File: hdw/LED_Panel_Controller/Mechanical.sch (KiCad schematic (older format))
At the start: 12 parts

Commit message: added digikey pns, footprints, bom scrubbed
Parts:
- MK? (x8): Configuration (none) -> DEV
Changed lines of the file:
@@
 F 3 "" H 4070 3910 50  0001 C CNN
 F 4 "1772-1220-ND" H 4070 3560 50  0001 C CNN "Digi-Key PN"
+F 5 "DEV" H 4070 3560 50  0001 C CNN "Configuration"
 	1    4070 3560
 	1    0    0    -1
@@
 F 3 "" H 4820 3910 50  0001 C CNN
 F 4 "1772-1220-ND" H 4820 3560 50  0001 C CNN "Digi-Key PN"
+F 5 "DEV" H 4820 3560 50  0001 C CNN "Configuration"
 	1    4820 3560
 	1    0    0    -1
@@
 F 3 "" H 4070 4410 50  0001 C CNN
 F 4 "1772-1220-ND" H 4070 4060 50  0001 C CNN "Digi-Key PN"
+F 5 "DEV" H 4070 4060 50  0001 C CNN "Configuration"
 	1    4070 4060
 	1    0    0    -1
@@
 F 3 "" H 4820 4410 50  0001 C CNN
 F 4 "1772-1220-ND" H 4820 4060 50  0001 C CNN "Digi-Key PN"
+F 5 "DEV" H 4820 4060 50  0001 C CNN "Configuration"
 	1    4820 4060
 	1    0    0    -1
@@
 F 3 "" H 4070 5920 50  0001 C CNN
 F 4 "36-9900-ND" H 4070 5670 50  0001 C CNN "Digi-Key PN"
+F 5 "DEV" H 4070 5670 50  0001 C CNN "Configuration"
 	1    4070 5670
 	1    0    0    -1
@@
 F 3 "" H 4820 5920 50  0001 C CNN
 F 4 "36-9900-ND" H 4820 5670 50  0001 C CNN "Digi-Key PN"
+F 5 "DEV" H 4820 5670 50  0001 C CNN "Configuration"
 	1    4820 5670
 	1    0    0    -1
@@
 F 3 "" H 4070 6420 50  0001 C CNN
 F 4 "36-9900-ND" H 4070 6170 50  0001 C CNN "Digi-Key PN"
+F 5 "DEV" H 4070 6170 50  0001 C CNN "Configuration"
 	1    4070 6170
 	1    0    0    -1
@@
 F 3 "" H 4820 6420 50  0001 C CNN
 F 4 "36-9900-ND" H 4820 6170 50  0001 C CNN "Digi-Key PN"
+F 5 "DEV" H 4820 6170 50  0001 C CNN "Configuration"
 	1    4820 6170
 	1    0    0    -1

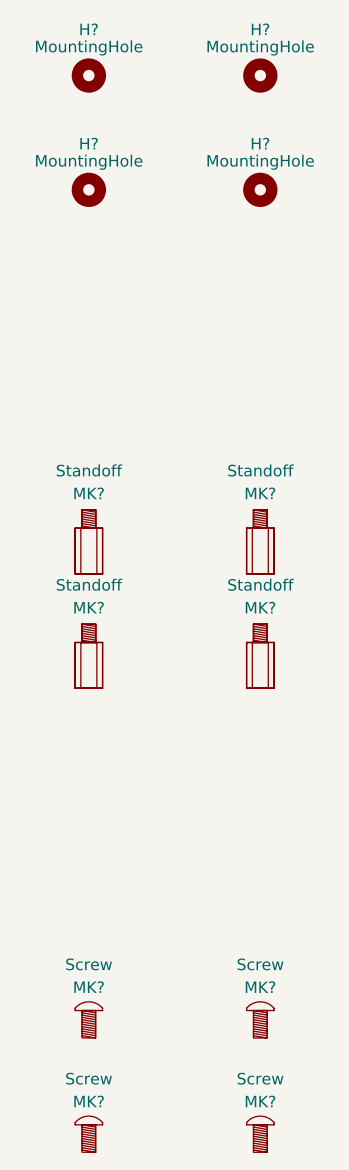
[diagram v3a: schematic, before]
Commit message: assigned I2C addresses
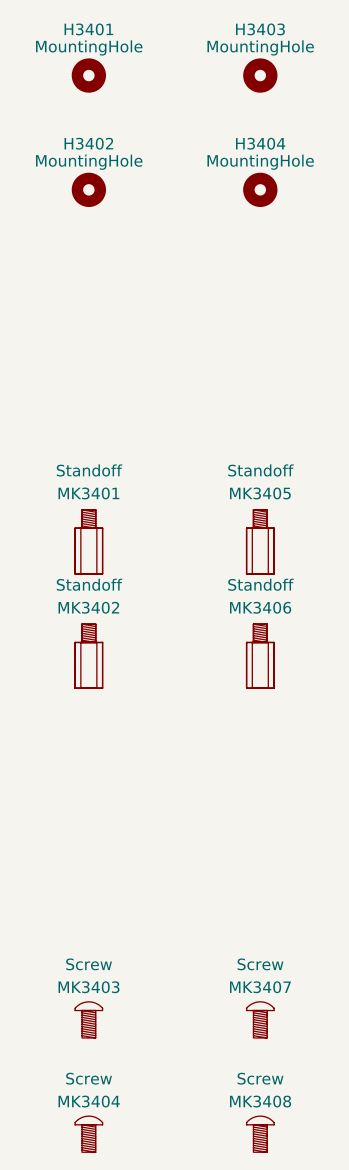
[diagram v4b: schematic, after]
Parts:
- gave numbers to parts that had none: 12
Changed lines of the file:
@@
 $EndDescr
 $Comp
-L Mechanical:MountingHole H?
+L Mechanical:MountingHole H3401
 U 1 1 5CC525BF
 P 4070 1580
-F 0 "H?" H 4070 1780 50  0000 C CNN
+F 0 "H3401" H 4070 1780 50  0000 C CNN
 F 1 "MountingHole" H 4070 1705 50  0000 C CNN
 F 2 "MountingHole:MountingHole_3mm" H 4070 1580 50  0001 C CNN
@@
 $EndComp
 $Comp
-L Mechanical:MountingHole H?
+L Mechanical:MountingHole H3403
 U 1 1 5CC5295F
 P 4820 1580
-F 0 "H?" H 4820 1780 50  0000 C CNN
+F 0 "H3403" H 4820 1780 50  0000 C CNN
 F 1 "MountingHole" H 4820 1705 50  0000 C CNN
 F 2 "MountingHole:MountingHole_3mm" H 4820 1580 50  0001 C CNN
@@
 $EndComp
 $Comp
-L Mechanical:MountingHole H?
+L Mechanical:MountingHole H3402
 U 1 1 5CC53950
 P 4070 2080
-F 0 "H?" H 4070 2280 50  0000 C CNN
+F 0 "H3402" H 4070 2280 50  0000 C CNN
 F 1 "MountingHole" H 4070 2205 50  0000 C CNN
 F 2 "MountingHole:MountingHole_3mm" H 4070 2080 50  0001 C CNN
@@
 $EndComp
 $Comp
-L Mechanical:MountingHole H?
+L Mechanical:MountingHole H3404
 U 1 1 5CC5395A
 P 4820 2080
-F 0 "H?" H 4820 2280 50  0000 C CNN
+F 0 "H3404" H 4820 2280 50  0000 C CNN
 F 1 "MountingHole" H 4820 2205 50  0000 C CNN
 F 2 "MountingHole:MountingHole_3mm" H 4820 2080 50  0001 C CNN
@@
 $EndComp
 $Comp
-L Custom_Library:Standoff MK?
+L Custom_Library:Standoff MK3401
 U 1 1 5CC60957
 P 4070 3560
-F 0 "MK?" H 4070 3710 50  0000 C CNN
+F 0 "MK3401" H 4070 3710 50  0000 C CNN
 F 1 "Standoff" H 4070 3810 50  0000 C CNN
 F 2 "" H 4070 3910 50  0001 C CNN
@@
 $EndComp
 $Comp
-L Custom_Library:Standoff MK?
+L Custom_Library:Standoff MK3405
 U 1 1 5CC60961
 P 4820 3560
-F 0 "MK?" H 4820 3710 50  0000 C CNN
+F 0 "MK3405" H 4820 3710 50  0000 C CNN
 F 1 "Standoff" H 4820 3810 50  0000 C CNN
 F 2 "" H 4820 3910 50  0001 C CNN
@@
 $EndComp
 $Comp
-L Custom_Library:Standoff MK?
+L Custom_Library:Standoff MK3402
 U 1 1 5CC6097F
 P 4070 4060
-F 0 "MK?" H 4070 4210 50  0000 C CNN
+F 0 "MK3402" H 4070 4210 50  0000 C CNN
 F 1 "Standoff" H 4070 4310 50  0000 C CNN
 F 2 "" H 4070 4410 50  0001 C CNN
@@
 $EndComp
 $Comp
-L Custom_Library:Standoff MK?
+L Custom_Library:Standoff MK3406
 U 1 1 5CC60989
 P 4820 4060
-F 0 "MK?" H 4820 4210 50  0000 C CNN
+F 0 "MK3406" H 4820 4210 50  0000 C CNN
 F 1 "Standoff" H 4820 4310 50  0000 C CNN
 F 2 "" H 4820 4410 50  0001 C CNN
@@
 $EndComp
 $Comp
-L Custom_Library:Screw MK?
+L Custom_Library:Screw MK3403
 U 1 1 5CC6CBF3
 P 4070 5670
-F 0 "MK?" H 4070 5770 50  0000 C CNN
+F 0 "MK3403" H 4070 5770 50  0000 C CNN
 F 1 "Screw" H 4070 5870 50  0000 C CNN
 F 2 "" H 4070 5920 50  0001 C CNN
@@
 $EndComp
 $Comp
-L Custom_Library:Screw MK?
+L Custom_Library:Screw MK3407
 U 1 1 5CC6D1A5
 P 4820 5670
-F 0 "MK?" H 4820 5770 50  0000 C CNN
+F 0 "MK3407" H 4820 5770 50  0000 C CNN
 F 1 "Screw" H 4820 5870 50  0000 C CNN
 F 2 "" H 4820 5920 50  0001 C CNN
@@
 $EndComp
 $Comp
-L Custom_Library:Screw MK?
+L Custom_Library:Screw MK3404
 U 1 1 5CC70A99
 P 4070 6170
-F 0 "MK?" H 4070 6270 50  0000 C CNN
+F 0 "MK3404" H 4070 6270 50  0000 C CNN
 F 1 "Screw" H 4070 6370 50  0000 C CNN
 F 2 "" H 4070 6420 50  0001 C CNN
@@
 $EndComp
 $Comp
-L Custom_Library:Screw MK?
+L Custom_Library:Screw MK3408
 U 1 1 5CC70AA3
 P 4820 6170
-F 0 "MK?" H 4820 6270 50  0000 C CNN
+F 0 "MK3408" H 4820 6270 50  0000 C CNN
 F 1 "Screw" H 4820 6370 50  0000 C CNN
 F 2 "" H 4820 6420 50  0001 C CNN
